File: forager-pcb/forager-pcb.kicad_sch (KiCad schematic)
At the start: 76 parts, among them J1 Conn_01x02_Pin, J2 Conn_01x02_Pin

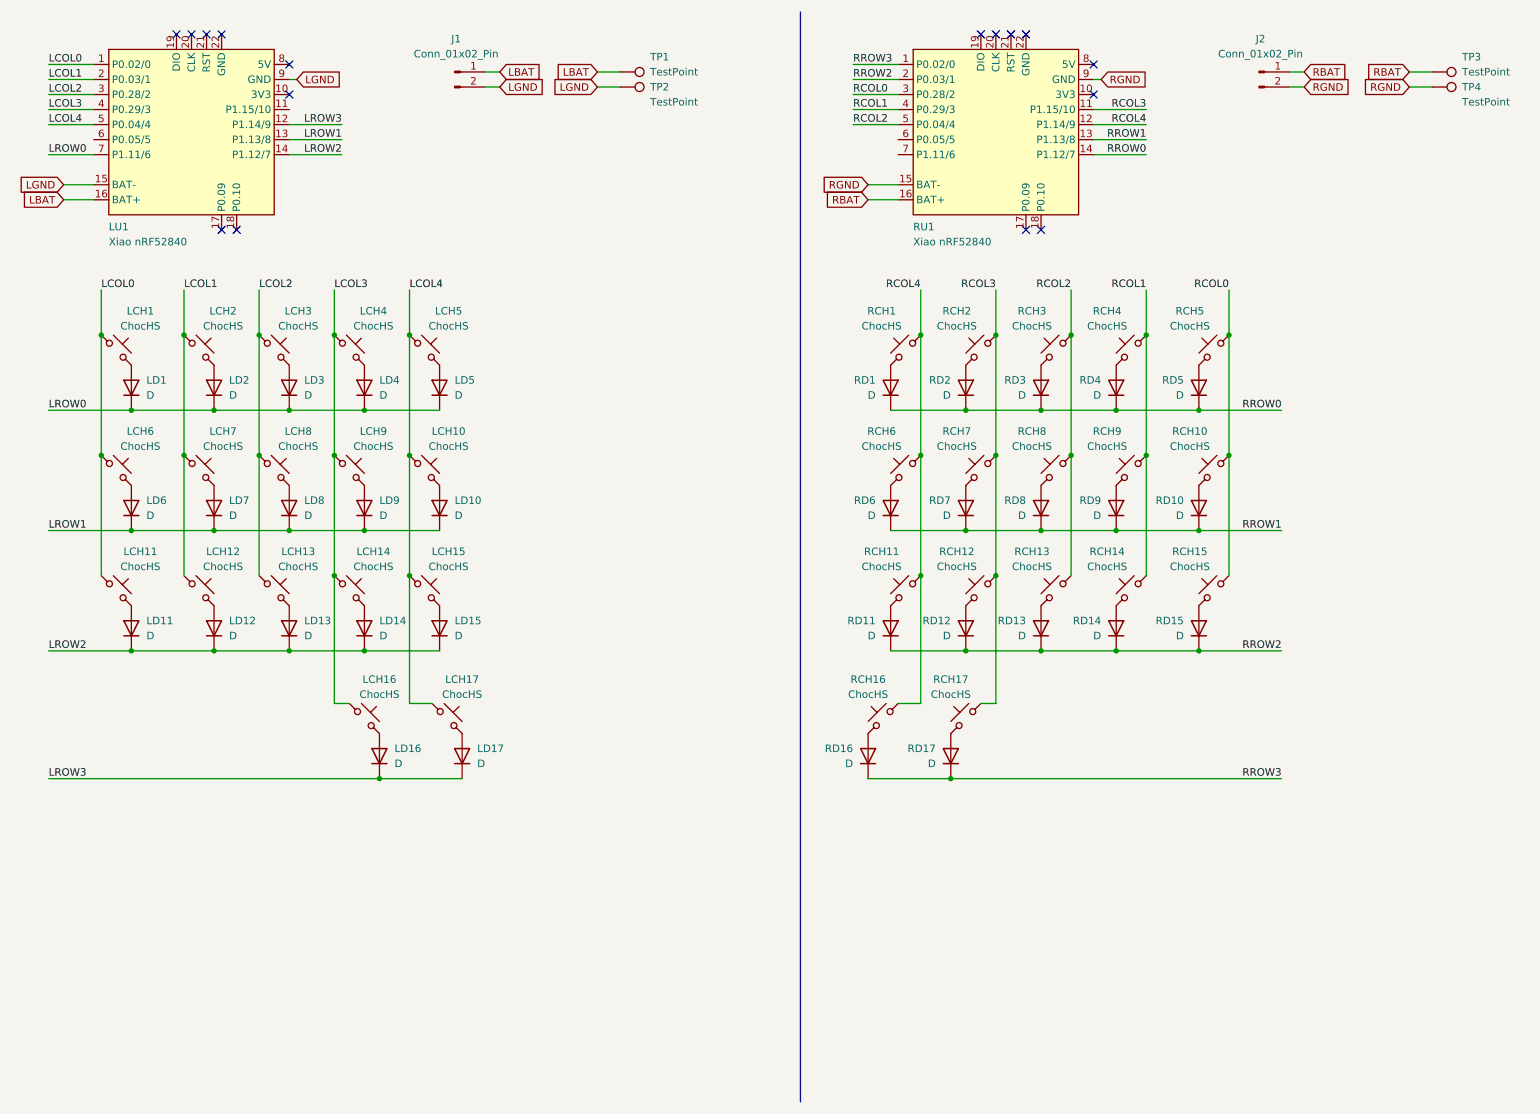
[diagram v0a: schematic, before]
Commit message: Add extra row to schematic and update PCB
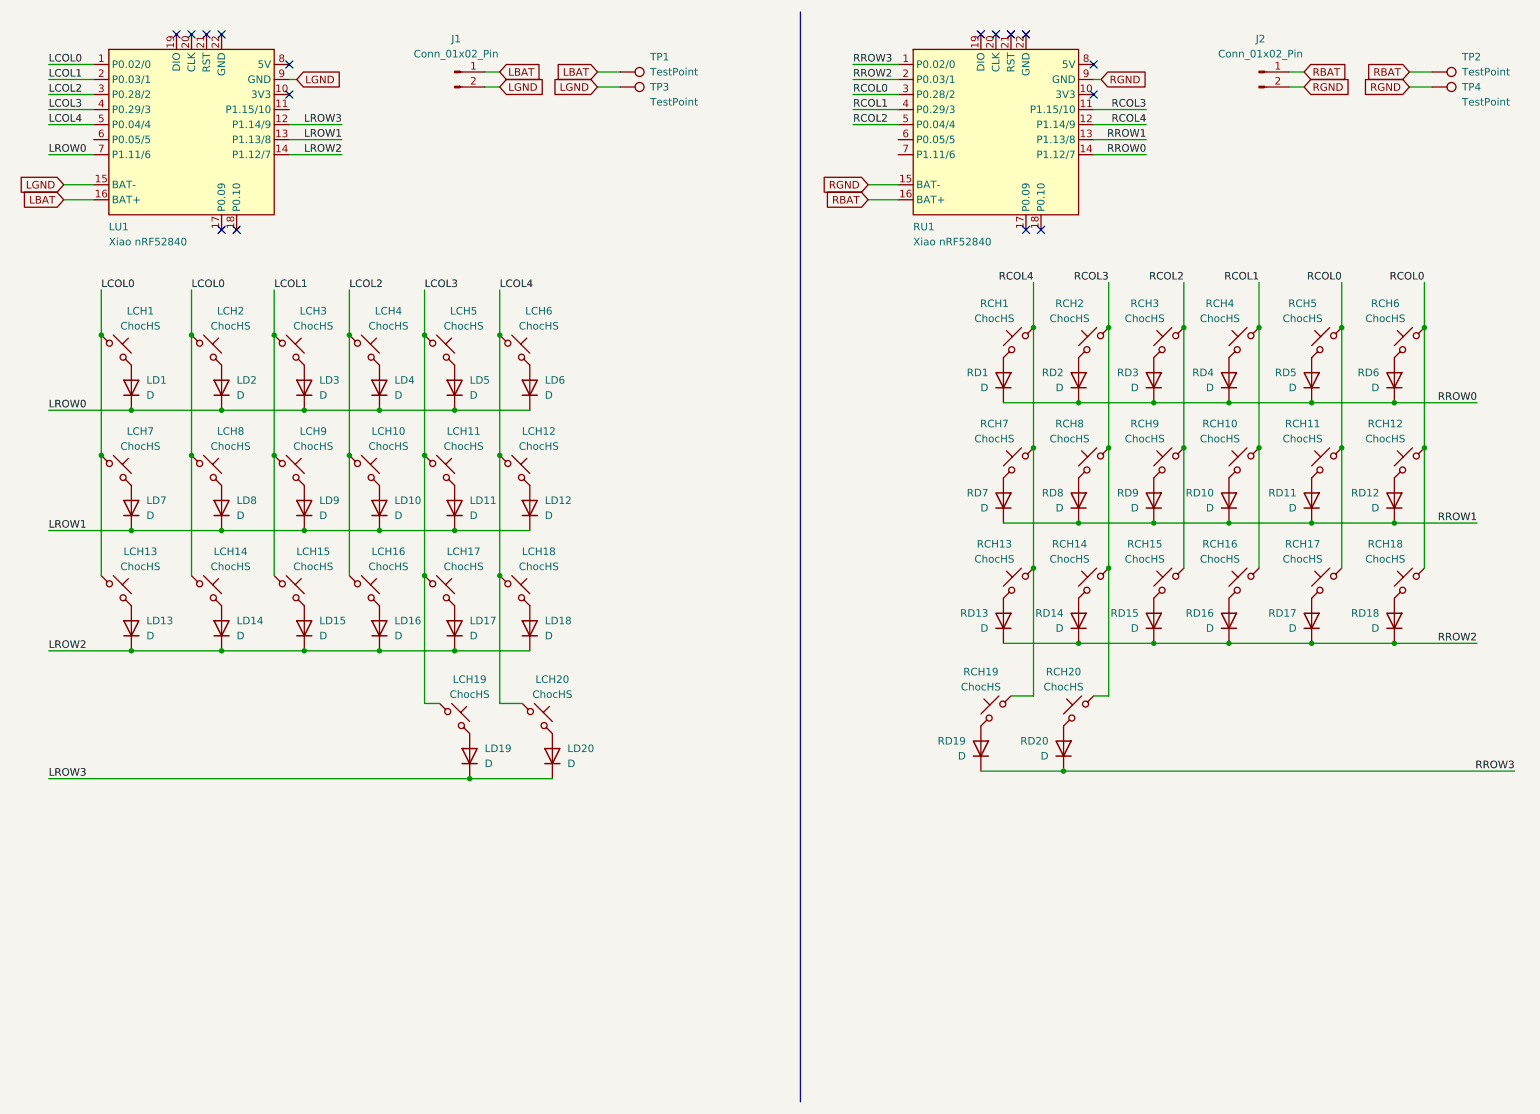
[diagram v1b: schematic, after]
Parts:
- added LCH14, LCH2, LCH8, RCH11, RCH17, RCH5: ChocHS, Custom:SW_choc_v1_HS_MBK, symbol Switch:SW_Push_45deg
- added LD14, LD2, LD8, RD11, RD17, RD5: D, Diode_SMD:D_SOD-123, symbol Device:D
- renumbered LCH8 to LCH10, LCH9 to LCH11, LCH10 to LCH12, LCH11 to LCH13, LCH12 to LCH15, LCH13 to LCH16, LCH14 to LCH17, LCH15 to LCH18, LCH16 to LCH19, LCH17 to LCH20, LCH2 to LCH3, LCH3 to LCH4, LCH4 to LCH5, LCH5 to LCH6, LCH6 to LCH7, LCH7 to LCH9, LD8 to LD10, LD9 to LD11, LD10 to LD12, LD11 to LD13, LD12 to LD15, LD13 to LD16, LD14 to LD17, LD15 to LD18, LD16 to LD19, LD17 to LD20, LD2 to LD3, LD3 to LD4, LD4 to LD5, LD5 to LD6, LD6 to LD7, LD7 to LD9, RCH9 to RCH10, RCH10 to RCH12, RCH11 to RCH13, RCH12 to RCH14, RCH13 to RCH15, RCH14 to RCH16, RCH15 to RCH18, RCH16 to RCH19, RCH17 to RCH20, RCH5 to RCH6, RCH6 to RCH7, RCH7 to RCH8, RCH8 to RCH9, RD9 to RD10, RD10 to RD12, RD11 to RD13, RD12 to RD14, RD13 to RD15, RD14 to RD16, RD15 to RD18, RD16 to RD19, RD17 to RD20, RD5 to RD6, RD6 to RD7, RD7 to RD8, RD8 to RD9, TP3 to TP2, TP2 to TP3
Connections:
- net LCOL0: now also LCH14.1, LCH2.1, LCH8.1
- net LROW0: now also LD2.1 (K)
- net LROW1: now also LD8.1 (K)
- net LROW2: now also LD14.1 (K)
- net RCOL0: now also RCH11.1, RCH17.1, RCH5.1
- net RROW0: now also RD5.1 (K)
- net RROW1: now also RD11.1 (K)
- net RROW2: now also RD17.1 (K)
- new net: RCH17.2, RD17.2 (A)
- new net: RCH5.2, RD5.2 (A)
- new net: RCH11.2, RD11.2 (A)
- new net: LCH8.2, LD8.2 (A)
- new net: LCH2.2, LD2.2 (A)
- new net: LCH14.2, LD14.2 (A)
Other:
- moved on the sheet: LCH10, LCH11, LCH12, LCH15, LCH16, LCH17, LCH18, LCH19, LCH20, LCH3, LCH4, LCH5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

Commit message: Fix bad annotation
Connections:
- net LCOL0: no longer LCH14.1, LCH2.1, LCH8.1
- net LCOL1: now also LCH14.1, LCH2.1, LCH8.1; no longer LCH15.1, LCH3.1, LCH9.1
- net LCOL2: now also LCH15.1, LCH3.1, LCH9.1; no longer LCH10.1, LCH16.1, LCH4.1
- net LCOL3: now also LCH10.1, LCH16.1, LCH4.1; no longer LCH11.1, LCH17.1, LCH19.1, LCH5.1
- net LCOL4: now also LCH11.1, LCH17.1, LCH19.1, LCH5.1; no longer LCH12.1, LCH18.1, LCH20.1, LCH6.1
- net RCOL0: no longer RCH11.1, RCH17.1, RCH5.1
- net RCOL1: now also RCH11.1, RCH17.1, RCH5.1; no longer RCH10.1, RCH16.1, RCH4.1
- net RCOL2: now also RCH10.1, RCH16.1, RCH4.1; no longer RCH15.1, RCH3.1, RCH9.1
- net RCOL3: now also RCH15.1, RCH3.1, RCH9.1, RU1.6 (P0.05/5); no longer RCH14.1, RCH2.1, RCH20.1, RCH8.1, RU1.11 (P1.15/10)
- net RCOL4: now also RCH14.1, RCH2.1, RCH20.1, RCH8.1, RU1.11 (P1.15/10); no longer RCH1.1, RCH13.1, RCH19.1, RCH7.1, RU1.12 (P1.14/9)
- net LCOL5: now reaches LU1.6 (P0.05/5)
- net LCOL5: now also LCH12.1, LCH18.1, LCH20.1, LCH6.1
- new net RCOL5: RCH1.1, RCH13.1, RCH19.1, RCH7.1, RU1.12 (P1.14/9)
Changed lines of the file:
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@@
+	(wire
+		(pts
+			(xy 20.32 34.29) (xy 27.94 34.29)
+		)
+		(stroke
+			(width 0)
+			(type default)
+		)
+	)
 	(wire
 		(pts
@@
 		(pts
 			(xy 186.69 86.36) (xy 186.69 106.68)
+		)
+		(stroke
+			(width 0)
+			(type default)
+		)
+	)
+	(wire
+		(pts
+			(xy 156.21 34.29) (xy 163.83 34.29)
 		)
 		(stroke
@@
 		)
 	)
-	(label "RCOL2"
+	(label "RCOL3"
 		(at 212.09 58.42 180)
 		(fields_autoplaced yes)
@@
 		)
 	)
-	(label "LCOL4"
+	(label "LCOL5"
 		(at 96.52 59.69 0)
 		(fields_autoplaced yes)
@@
 		)
 	)
-	(label "RCOL4"
+	(label "RCOL5"
 		(at 205.74 31.75 180)
 		(fields_autoplaced yes)
@@
 		)
 	)
-	(label "RCOL3"
+	(label "RCOL4"
 		(at 205.74 29.21 180)
 		(fields_autoplaced yes)
@@
 		)
 	)
-	(label "RCOL1"
+	(label "RCOL2"
 		(at 224.79 58.42 180)
 		(fields_autoplaced yes)
@@
 		)
 	)
-	(label "LCOL2"
+	(label "LCOL3"
 		(at 71.12 59.69 0)
 		(fields_autoplaced yes)
@@
 		)
 	)
-	(label "RCOL0"
+	(label "RCOL1"
 		(at 238.76 58.42 180)
 		(fields_autoplaced yes)
@@
 		)
 	)
-	(label "LCOL0"
+	(label "LCOL1"
 		(at 44.45 59.69 0)
 		(fields_autoplaced yes)
@@
 		)
 	)
-	(label "LCOL3"
+	(label "LCOL5"
+		(at 20.32 34.29 0)
+		(fields_autoplaced yes)
+		(effects
+			(font
+				(size 1.27 1.27)
+			)
+			(justify left bottom)
+		)
+	)
+	(label "LCOL4"
 		(at 83.82 59.69 0)
 		(fields_autoplaced yes)
@@
 		)
 	)
-	(label "RCOL4"
+	(label "RCOL5"
 		(at 186.69 58.42 180)
 		(fields_autoplaced yes)
@@
 			)
 			(justify right bottom)
+		)
+	)
+	(label "RCOL3"
+		(at 156.21 34.29 0)
+		(fields_autoplaced yes)
+		(effects
+			(font
+				(size 1.27 1.27)
+			)
+			(justify left bottom)
 		)
 	)
@@
 		)
 	)
-	(label "LCOL1"
+	(label "LCOL2"
 		(at 58.42 59.69 0)
 		(fields_autoplaced yes)
@@
 		)
 	)
-	(label "RCOL3"
+	(label "RCOL4"
 		(at 199.39 58.42 180)
 		(fields_autoplaced yes)

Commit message: Swap to choc v2 comparible centerhole
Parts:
- LCH1, LCH10, LCH11, LCH12, LCH13, LCH14, LCH15, LCH16, LCH17, LCH18, LCH19, LCH2, LCH20, LCH3, LCH4, LCH5, LCH6, LCH7, LCH8, LCH9, RCH1, RCH10, RCH11, RCH12, RCH13, RCH14, RCH15, RCH16, RCH17, RCH18, RCH19, RCH2, RCH20, RCH3, RCH4, RCH5, RCH6, RCH7, RCH8, RCH9: footprint Custom:SW_choc_v1_HS_MBK -> Custom:SW_choc_v1v2_HS_MBK
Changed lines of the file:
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@@
 			)
 		)
-		(property "Footprint" "Custom:SW_choc_v1_HS_MBK"
+		(property "Footprint" "Custom:SW_choc_v1v2_HS_MBK"
 			(at 236.22 109.22 0)
 			(effects
@@
 			)
 		)
-		(property "Footprint" "Custom:SW_choc_v1_HS_MBK"
+		(property "Footprint" "Custom:SW_choc_v1v2_HS_MBK"
 			(at 31.75 90.17 0)
 			(effects
@@
 			)
 		)
-		(property "Footprint" "Custom:SW_choc_v1_HS_MBK"
+		(property "Footprint" "Custom:SW_choc_v1v2_HS_MBK"
 			(at 86.36 110.49 0)
 			(effects
@@
 			)
 		)
-		(property "Footprint" "Custom:SW_choc_v1_HS_MBK"
+		(property "Footprint" "Custom:SW_choc_v1v2_HS_MBK"
 			(at 236.22 68.58 0)
 			(effects
@@
 			)
 		)
-		(property "Footprint" "Custom:SW_choc_v1_HS_MBK"
+		(property "Footprint" "Custom:SW_choc_v1v2_HS_MBK"
 			(at 73.66 90.17 0)
 			(effects
@@
 			)
 		)
-		(property "Footprint" "Custom:SW_choc_v1_HS_MBK"
+		(property "Footprint" "Custom:SW_choc_v1v2_HS_MBK"
 			(at 184.15 88.9 0)
 			(effects
@@
 			)
 		)
-		(property "Footprint" "Custom:SW_choc_v1_HS_MBK"
+		(property "Footprint" "Custom:SW_choc_v1v2_HS_MBK"
 			(at 46.99 69.85 0)
 			(effects
@@
 			)
 		)
-		(property "Footprint" "Custom:SW_choc_v1_HS_MBK"
+		(property "Footprint" "Custom:SW_choc_v1v2_HS_MBK"
 			(at 209.55 109.22 0)
 			(effects
@@
 			)
 		)
-		(property "Footprint" "Custom:SW_choc_v1_HS_MBK"
+		(property "Footprint" "Custom:SW_choc_v1v2_HS_MBK"
 			(at 184.15 68.58 0)
 			(effects
@@
 			)
 		)
-		(property "Footprint" "Custom:SW_choc_v1_HS_MBK"
+		(property "Footprint" "Custom:SW_choc_v1v2_HS_MBK"
 			(at 73.66 110.49 0)
 			(effects
@@
 			)
 		)
-		(property "Footprint" "Custom:SW_choc_v1_HS_MBK"
+		(property "Footprint" "Custom:SW_choc_v1v2_HS_MBK"
 			(at 196.85 68.58 0)
 			(effects
@@
 			)
 		)
-		(property "Footprint" "Custom:SW_choc_v1_HS_MBK"
+		(property "Footprint" "Custom:SW_choc_v1v2_HS_MBK"
 			(at 180.34 130.81 0)
 			(effects
@@
 			)
 		)
-		(property "Footprint" "Custom:SW_choc_v1_HS_MBK"
+		(property "Footprint" "Custom:SW_choc_v1v2_HS_MBK"
 			(at 209.55 68.58 0)
 			(effects
@@
 			)
 		)
-		(property "Footprint" "Custom:SW_choc_v1_HS_MBK"
+		(property "Footprint" "Custom:SW_choc_v1v2_HS_MBK"
 			(at 86.36 90.17 0)
 			(effects
@@
 			)
 		)
-		(property "Footprint" "Custom:SW_choc_v1_HS_MBK"
+		(property "Footprint" "Custom:SW_choc_v1v2_HS_MBK"
 			(at 73.66 69.85 0)
 			(effects
@@
 			)
 		)
-		(property "Footprint" "Custom:SW_choc_v1_HS_MBK"
+		(property "Footprint" "Custom:SW_choc_v1v2_HS_MBK"
 			(at 60.96 69.85 0)
 			(effects
@@
 			)
 		)
-		(property "Footprint" "Custom:SW_choc_v1_HS_MBK"
+		(property "Footprint" "Custom:SW_choc_v1v2_HS_MBK"
 			(at 102.87 132.08 0)
 			(effects
@@
 			)
 		)
-		(property "Footprint" "Custom:SW_choc_v1_HS_MBK"
+		(property "Footprint" "Custom:SW_choc_v1v2_HS_MBK"
 			(at 86.36 69.85 0)
 			(effects
@@
 			)
 		)
-		(property "Footprint" "Custom:SW_choc_v1_HS_MBK"
+		(property "Footprint" "Custom:SW_choc_v1v2_HS_MBK"
 			(at 236.22 88.9 0)
 			(effects
@@
 			)
 		)
-		(property "Footprint" "Custom:SW_choc_v1_HS_MBK"
+		(property "Footprint" "Custom:SW_choc_v1v2_HS_MBK"
 			(at 196.85 88.9 0)
 			(effects
@@
 			)
 		)
-		(property "Footprint" "Custom:SW_choc_v1_HS_MBK"
+		(property "Footprint" "Custom:SW_choc_v1v2_HS_MBK"
 			(at 209.55 88.9 0)
 			(effects
@@
 			)
 		)
-		(property "Footprint" "Custom:SW_choc_v1_HS_MBK"
+		(property "Footprint" "Custom:SW_choc_v1v2_HS_MBK"
 			(at 222.25 88.9 0)
 			(effects
@@
 			)
 		)
-		(property "Footprint" "Custom:SW_choc_v1_HS_MBK"
+		(property "Footprint" "Custom:SW_choc_v1v2_HS_MBK"
 			(at 88.9 132.08 0)
 			(effects
@@
 			)
 		)
-		(property "Footprint" "Custom:SW_choc_v1_HS_MBK"
+		(property "Footprint" "Custom:SW_choc_v1v2_HS_MBK"
 			(at 31.75 110.49 0)
 			(effects
@@
 			)
 		)
-		(property "Footprint" "Custom:SW_choc_v1_HS_MBK"
+		(property "Footprint" "Custom:SW_choc_v1v2_HS_MBK"
 			(at 99.06 69.85 0)
 			(effects
@@
 			)
 		)
-		(property "Footprint" "Custom:SW_choc_v1_HS_MBK"
+		(property "Footprint" "Custom:SW_choc_v1v2_HS_MBK"
 			(at 184.15 109.22 0)
 			(effects
@@
 			)
 		)
-		(property "Footprint" "Custom:SW_choc_v1_HS_MBK"
+		(property "Footprint" "Custom:SW_choc_v1v2_HS_MBK"
 			(at 46.99 110.49 0)
 			(effects
@@
 			)
 		)
-		(property "Footprint" "Custom:SW_choc_v1_HS_MBK"
+		(property "Footprint" "Custom:SW_choc_v1v2_HS_MBK"
 			(at 250.19 109.22 0)
 			(effects
@@
 			)
 		)
-		(property "Footprint" "Custom:SW_choc_v1_HS_MBK"
+		(property "Footprint" "Custom:SW_choc_v1v2_HS_MBK"
 			(at 222.25 109.22 0)
 			(effects
@@
 			)
 		)
-		(property "Footprint" "Custom:SW_choc_v1_HS_MBK"
+		(property "Footprint" "Custom:SW_choc_v1v2_HS_MBK"
 			(at 196.85 109.22 0)
 			(effects
@@
 			)
 		)
-		(property "Footprint" "Custom:SW_choc_v1_HS_MBK"
+		(property "Footprint" "Custom:SW_choc_v1v2_HS_MBK"
 			(at 250.19 88.9 0)
 			(effects
@@
 			)
 		)
-		(property "Footprint" "Custom:SW_choc_v1_HS_MBK"
+		(property "Footprint" "Custom:SW_choc_v1v2_HS_MBK"
 			(at 99.06 90.17 0)
 			(effects
@@
 			)
 		)
-		(property "Footprint" "Custom:SW_choc_v1_HS_MBK"
+		(property "Footprint" "Custom:SW_choc_v1v2_HS_MBK"
 			(at 222.25 68.58 0)
 			(effects
@@
 			)
 		)
-		(property "Footprint" "Custom:SW_choc_v1_HS_MBK"
+		(property "Footprint" "Custom:SW_choc_v1v2_HS_MBK"
 			(at 194.31 130.81 0)
 			(effects
@@
 			)
 		)
-		(property "Footprint" "Custom:SW_choc_v1_HS_MBK"
+		(property "Footprint" "Custom:SW_choc_v1v2_HS_MBK"
 			(at 99.06 110.49 0)
 			(effects
@@
 			)
 		)
-		(property "Footprint" "Custom:SW_choc_v1_HS_MBK"
+		(property "Footprint" "Custom:SW_choc_v1v2_HS_MBK"
 			(at 31.75 69.85 0)
 			(effects
@@
 			)
 		)
-		(property "Footprint" "Custom:SW_choc_v1_HS_MBK"
+		(property "Footprint" "Custom:SW_choc_v1v2_HS_MBK"
 			(at 60.96 110.49 0)
 			(effects
@@
 			)
 		)
-		(property "Footprint" "Custom:SW_choc_v1_HS_MBK"
+		(property "Footprint" "Custom:SW_choc_v1v2_HS_MBK"
 			(at 250.19 68.58 0)
 			(effects
@@
 			)
 		)
-		(property "Footprint" "Custom:SW_choc_v1_HS_MBK"
+		(property "Footprint" "Custom:SW_choc_v1v2_HS_MBK"
 			(at 60.96 90.17 0)
 			(effects
@@
 			)
 		)
-		(property "Footprint" "Custom:SW_choc_v1_HS_MBK"
+		(property "Footprint" "Custom:SW_choc_v1v2_HS_MBK"
 			(at 46.99 90.17 0)
 			(effects
